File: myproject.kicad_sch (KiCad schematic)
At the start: 1 part

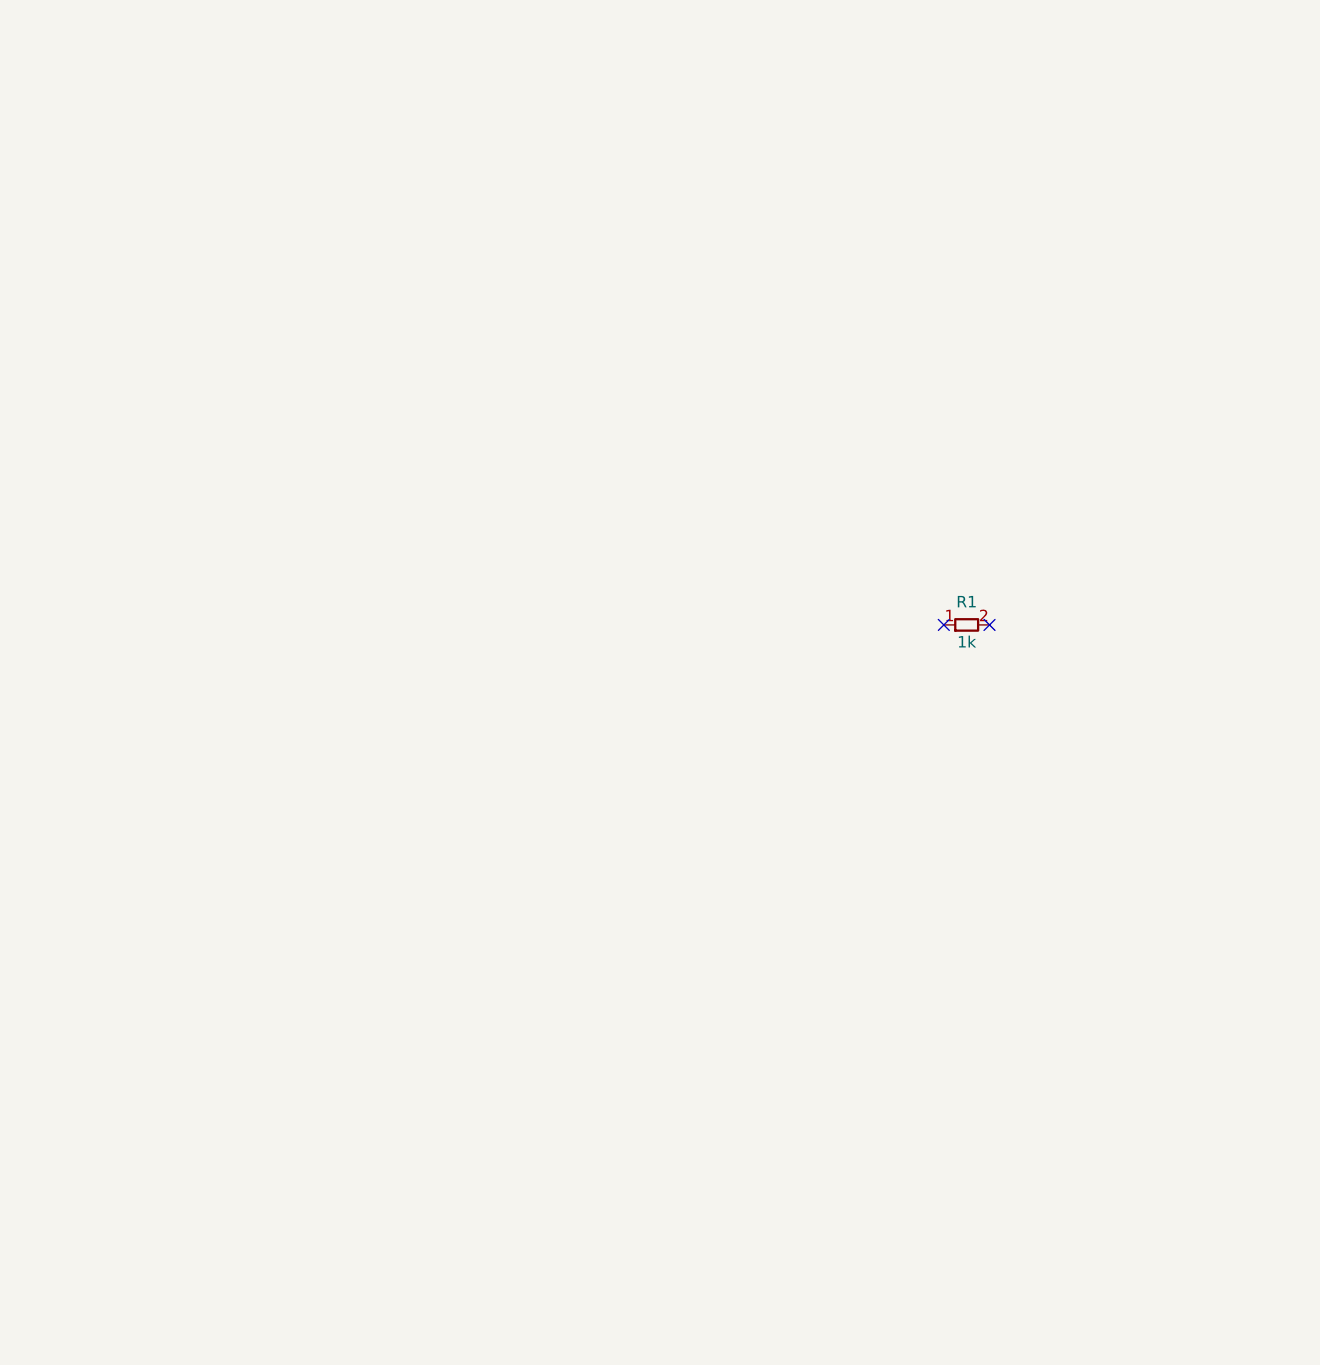
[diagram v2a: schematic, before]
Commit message: feat: Generate valid KiCad schematic for NE555 blinker
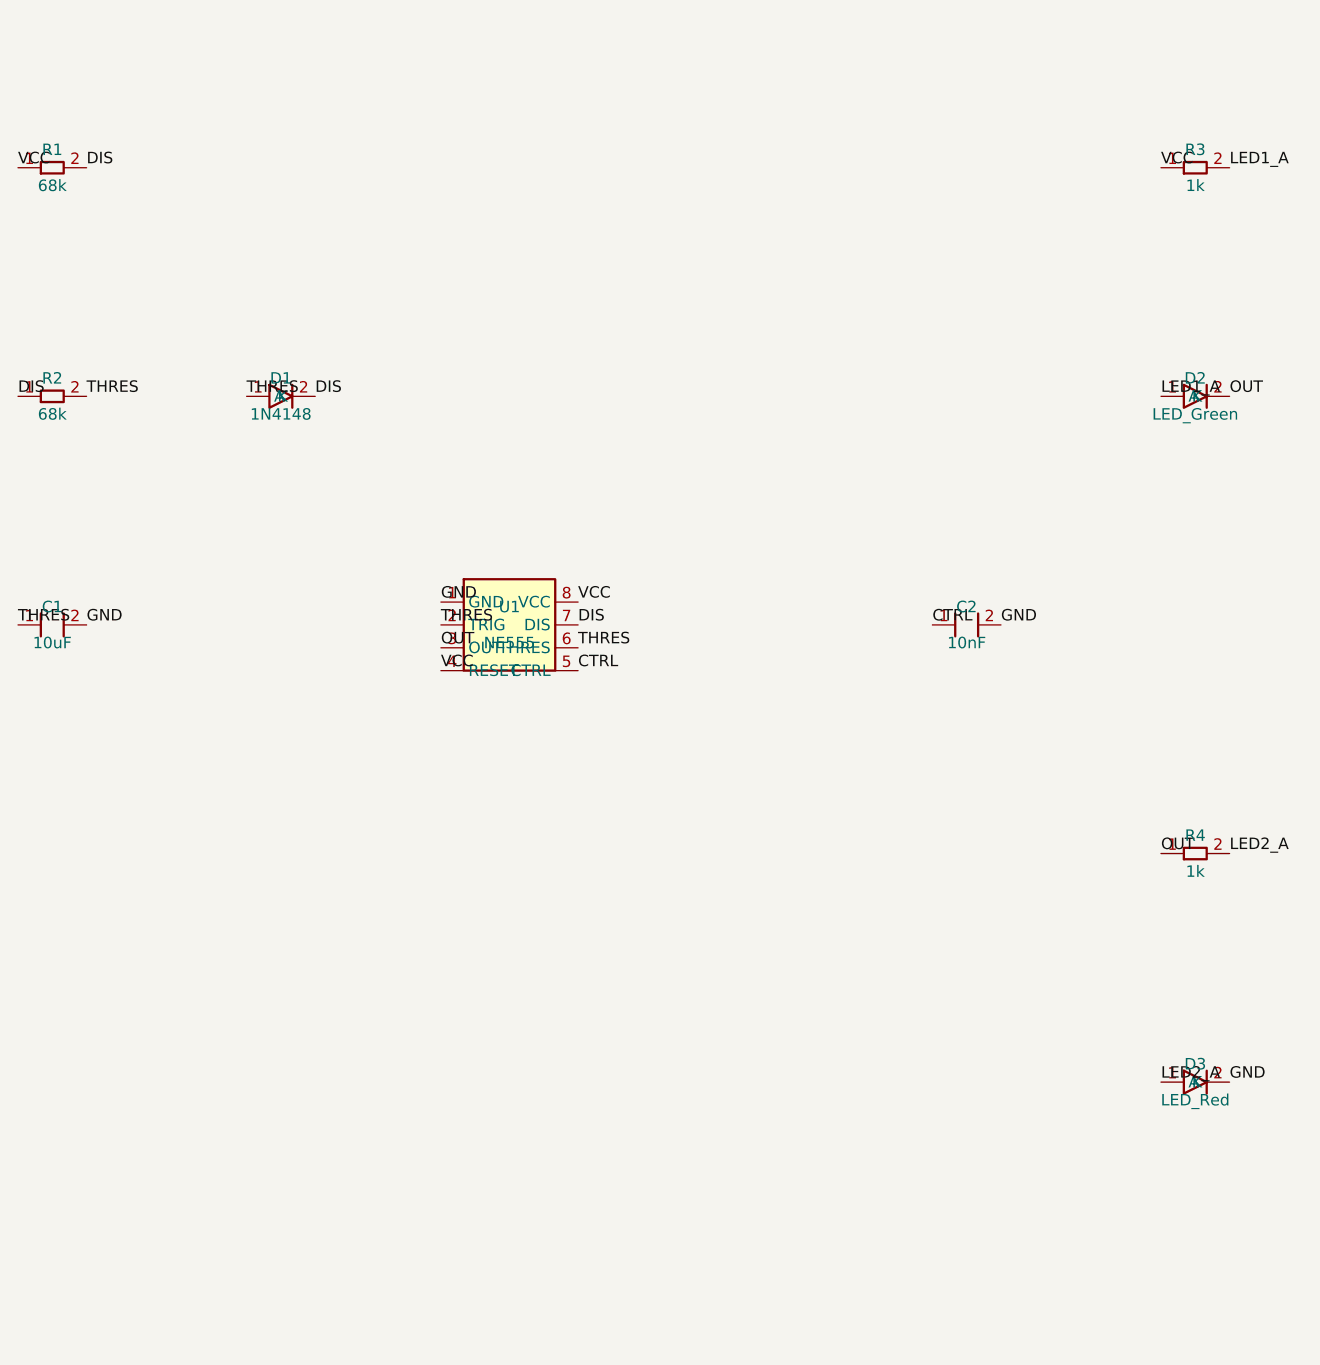
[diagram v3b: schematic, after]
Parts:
- added C1: 10uF, symbol Device:C
- added C2: 10nF, symbol Device:C
- added D1: 1N4148, symbol Device:D
- added D2: LED_Green, symbol Device:D
- added D3: LED_Red, symbol Device:D
- added R2: 68k, symbol Device:R
- added R3, R4: 1k, symbol Device:R
- added U1: NE555, symbol Timer:NE555
- R1: value 1k -> 68k
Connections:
- net VCC: now reaches R1.1
- net VCC: now also R3.1, U1.4 (RESET), U1.8 (VCC)
- net DIS: now reaches R1.2
- net DIS: now also D1.2 (K), R2.1, U1.7 (DIS)
- new net CTRL: C2.1, U1.5 (CTRL)
- new net GND: C1.2, C2.2, D3.2 (K), U1.1 (GND)
- new net LED1_A: D2.1 (A), R3.2
- new net LED2_A: D3.1 (A), R4.2
- new net OUT: D2.2 (K), R4.1, U1.3 (OUT)
- new net THRES: C1.1, D1.1 (A), R2.2, U1.2 (TRIG), U1.6 (THRES)
- no-connect marks 2 -> 0
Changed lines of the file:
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@@
   (version 20240702)
   (generator "Jules")
+  (paper "A4")
+  (symbol
+    (lib_id "Timer:NE555")
+    (at 101.6 101.6 0)
+    (unit 1)
+    (in_bom yes)
+    (on_board yes)
+    (property "Reference" "U1" (at 101.6 99.6 0) (effects (font (size 1.27 1.27))))
+    (property "Value" "NE555" (at 101.6 103.6 0) (effects (font (size 1.27 1.27))))
+  )
+  (label "GND" (at 93.98 99.06 0)
+    (effects (font (size 1.27 1.27)) (justify left bottom))
+  )
+  (label "THRES" (at 93.98 101.6 0)
+    (effects (font (size 1.27 1.27)) (justify left bottom))
+  )
+  (label "OUT" (at 93.98 104.14 0)
+    (effects (font (size 1.27 1.27)) (justify left bottom))
+  )
+  (label "VCC" (at 93.98 106.68 0)
+    (effects (font (size 1.27 1.27)) (justify left bottom))
+  )
+  (label "CTRL" (at 109.22 106.68 0)
+    (effects (font (size 1.27 1.27)) (justify left bottom))
+  )
+  (label "THRES" (at 109.22 104.14 0)
+    (effects (font (size 1.27 1.27)) (justify left bottom))
+  )
+  (label "DIS" (at 109.22 101.6 0)
+    (effects (font (size 1.27 1.27)) (justify left bottom))
+  )
+  (label "VCC" (at 109.22 99.06 0)
+    (effects (font (size 1.27 1.27)) (justify left bottom))
+  )
   (symbol
     (lib_id "Device:R")
+    (at 50.8 50.8 0)
+    (unit 1)
+    (in_bom yes)
+    (on_board yes)
+    (property "Reference" "R1" (at 50.8 48.8 0) (effects (font (size 1.27 1.27))))
+    (property "Value" "68k" (at 50.8 52.8 0) (effects (font (size 1.27 1.27))))
+  )
+  (label "VCC" (at 46.99 50.8 0)
+    (effects (font (size 1.27 1.27)) (justify left bottom))
+  )
+  (label "DIS" (at 54.61 50.8 0)
+    (effects (font (size 1.27 1.27)) (justify left bottom))
+  )
+  (symbol
+    (lib_id "Device:R")
+    (at 50.8 76.2 0)
+    (unit 1)
+    (in_bom yes)
+    (on_board yes)
+    (property "Reference" "R2" (at 50.8 74.2 0) (effects (font (size 1.27 1.27))))
+    (property "Value" "68k" (at 50.8 78.2 0) (effects (font (size 1.27 1.27))))
+  )
+  (label "DIS" (at 46.99 76.2 0)
+    (effects (font (size 1.27 1.27)) (justify left bottom))
+  )
+  (label "THRES" (at 54.61 76.2 0)
+    (effects (font (size 1.27 1.27)) (justify left bottom))
+  )
+  (symbol
+    (lib_id "Device:D")
+    (at 76.2 76.2 0)
+    (unit 1)
+    (in_bom yes)
+    (on_board yes)
+    (property "Reference" "D1" (at 76.2 74.2 0) (effects (font (size 1.27 1.27))))
+    (property "Value" "1N4148" (at 76.2 78.2 0) (effects (font (size 1.27 1.27))))
+  )
+  (label "THRES" (at 72.39 76.2 0)
+    (effects (font (size 1.27 1.27)) (justify left bottom))
+  )
+  (label "DIS" (at 80.01 76.2 0)
+    (effects (font (size 1.27 1.27)) (justify left bottom))
+  )
+  (symbol
+    (lib_id "Device:C")
+    (at 50.8 101.6 0)
+    (unit 1)
+    (in_bom yes)
+    (on_board yes)
+    (property "Reference" "C1" (at 50.8 99.6 0) (effects (font (size 1.27 1.27))))
+    (property "Value" "10uF" (at 50.8 103.6 0) (effects (font (size 1.27 1.27))))
+  )
+  (label "THRES" (at 46.99 101.6 0)
+    (effects (font (size 1.27 1.27)) (justify left bottom))
+  )
+  (label "GND" (at 54.61 101.6 0)
+    (effects (font (size 1.27 1.27)) (justify left bottom))
+  )
+  (symbol
+    (lib_id "Device:C")
     (at 152.4 101.6 0)
     (unit 1)
     (in_bom yes)
     (on_board yes)
-    (property "Reference" "R1" (at 152.4 99.06 0)
-      (effects (font (size 1.27 1.27)))
-    )
-    (property "Value" "1k" (at 152.4 103.52 0)
-      (effects (font (size 1.27 1.27)))
-    )
+    (property "Reference" "C2" (at 152.4 99.6 0) (effects (font (size 1.27 1.27))))
+    (property "Value" "10nF" (at 152.4 103.6 0) (effects (font (size 1.27 1.27))))
   )
-  (no_connect (at 149.86 101.6))
-  (no_connect (at 154.94 101.6))
+  (label "CTRL" (at 148.59 101.6 0)
+    (effects (font (size 1.27 1.27)) (justify left bottom))
+  )
+  (label "GND" (at 156.21 101.6 0)
+    (effects (font (size 1.27 1.27)) (justify left bottom))
+  )
+  (symbol
+    (lib_id "Device:R")
+    (at 177.8 50.8 0)
+    (unit 1)
+    (in_bom yes)
+    (on_board yes)
+    (property "Reference" "R3" (at 177.8 48.8 0) (effects (font (size 1.27 1.27))))
+    (property "Value" "1k" (at 177.8 52.8 0) (effects (font (size 1.27 1.27))))
+  )
+  (label "VCC" (at 173.99 50.8 0)
+    (effects (font (size 1.27 1.27)) (justify left bottom))
+  )
+  (label "LED1_A" (at 181.61 50.8 0)
+    (effects (font (size 1.27 1.27)) (justify left bottom))
+  )
+  (symbol
+    (lib_id "Device:D")
+    (at 177.8 76.2 0)
+    (unit 1)
+    (in_bom yes)
+    (on_board yes)
+    (property "Reference" "D2" (at 177.8 74.2 0) (effects (font (size 1.27 1.27))))
+    (property "Value" "LED_Green" (at 177.8 78.2 0) (effects (font (size 1.27 1.27))))
+  )
+  (label "LED1_A" (at 173.99 76.2 0)
+    (effects (font (size 1.27 1.27)) (justify left bottom))
+  )
+  (label "OUT" (at 181.61 76.2 0)
+    (effects (font (size 1.27 1.27)) (justify left bottom))
+  )
+  (symbol
+    (lib_id "Device:R")
+    (at 177.8 127.0 0)
+    (unit 1)
+    (in_bom yes)
+    (on_board yes)
+    (property "Reference" "R4" (at 177.8 125.0 0) (effects (font (size 1.27 1.27))))
+    (property "Value" "1k" (at 177.8 129.0 0) (effects (font (size 1.27 1.27))))
+  )
+  (label "OUT" (at 173.99 127.0 0)
+    (effects (font (size 1.27 1.27)) (justify left bottom))
+  )
+  (label "LED2_A" (at 181.61 127.0 0)
+    (effects (font (size 1.27 1.27)) (justify left bottom))
+  )
+  (symbol
+    (lib_id "Device:D")
+    (at 177.8 152.4 0)
+    (unit 1)
+    (in_bom yes)
+    (on_board yes)
+    (property "Reference" "D3" (at 177.8 150.4 0) (effects (font (size 1.27 1.27))))
+    (property "Value" "LED_Red" (at 177.8 154.4 0) (effects (font (size 1.27 1.27))))
+  )
+  (label "LED2_A" (at 173.99 152.4 0)
+    (effects (font (size 1.27 1.27)) (justify left bottom))
+  )
+  (label "GND" (at 181.61 152.4 0)
+    (effects (font (size 1.27 1.27)) (justify left bottom))
+  )
 )
